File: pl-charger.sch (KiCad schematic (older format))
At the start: 16 parts

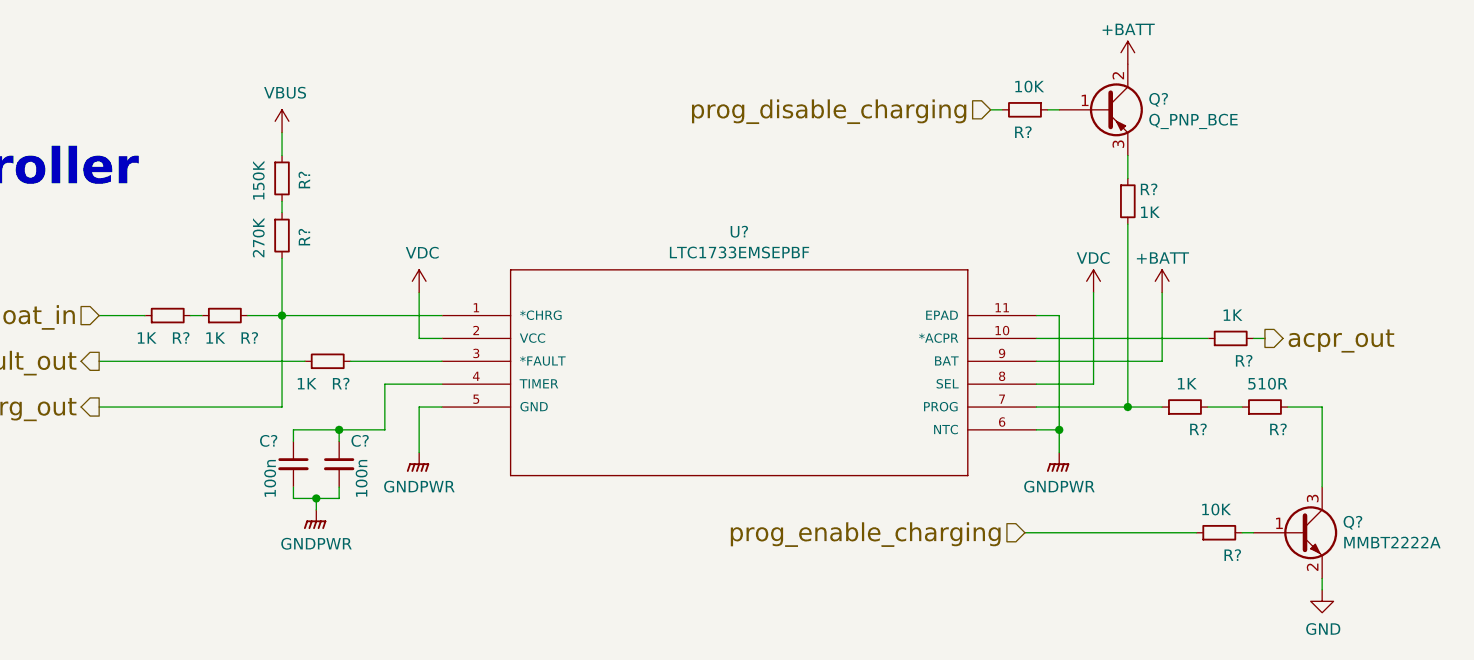
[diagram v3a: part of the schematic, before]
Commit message: Added component values
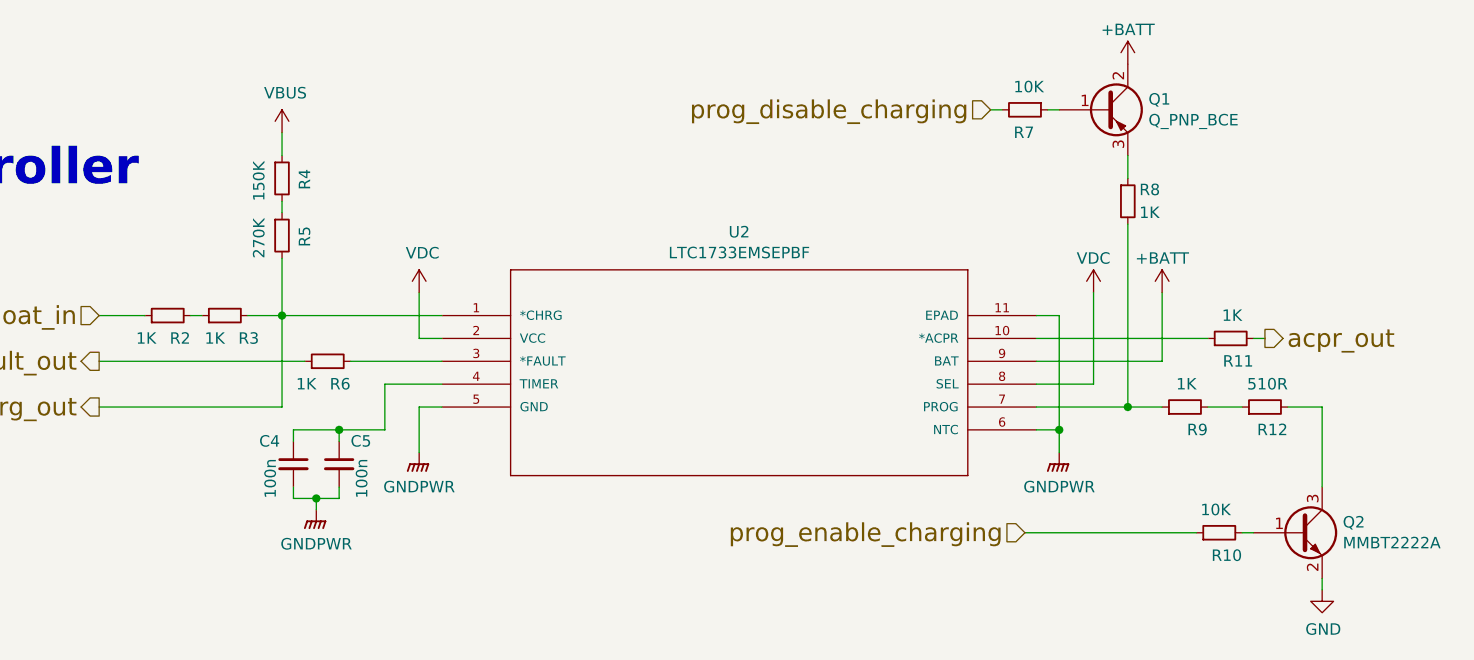
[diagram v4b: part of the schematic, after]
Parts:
- gave numbers to parts that had none: 16
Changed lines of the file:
@@
 $EndDescr
 $Comp
-L portable-light-rescue:R_Small-Device R?
+L portable-light-rescue:R_Small-Device R2
 U 1 1 5F378F6B
 P 3150 3500
-F 0 "R?" V 3050 3400 50  0000 L CNN
+F 0 "R2" V 3050 3400 50  0000 L CNN
 F 1 "1K" V 3050 3550 50  0000 L CNN
 F 2 "Resistor_SMD:R_0603_1608Metric_Pad1.05x0.95mm_HandSolder" H 3150 3500 50  0001 C CNN
@@
 $EndComp
 $Comp
-L portable-light-rescue:R_Small-Device R?
+L portable-light-rescue:R_Small-Device R3
 U 1 1 5F54FED1
 P 3400 3500
-F 0 "R?" V 3300 3350 50  0000 L CNN
+F 0 "R3" V 3300 3350 50  0000 L CNN
 F 1 "1K" V 3300 3500 50  0000 L CNN
 F 2 "Resistor_SMD:R_0603_1608Metric_Pad1.05x0.95mm_HandSolder" H 3400 3500 50  0001 C CNN
@@
 $EndComp
 $Comp
-L portable-light-rescue:VBUS-power #PWR?
+L portable-light-rescue:VBUS-power #PWR020
 U 1 1 5F15EA3E
 P 3650 2700
-F 0 "#PWR?" H 3650 2550 50  0001 C CNN
+F 0 "#PWR020" H 3650 2550 50  0001 C CNN
 F 1 "VBUS" H 3665 2873 50  0000 C CNN
 F 2 "" H 3650 2700 50  0001 C CNN
@@
 	2850 3500 3050 3500
 $Comp
-L portable-light-rescue:VDC-power #PWR?
+L portable-light-rescue:VDC-power #PWR022
 U 1 1 5F378F81
 P 4250 3400
-F 0 "#PWR?" H 4250 3300 50  0001 C CNN
+F 0 "#PWR022" H 4250 3300 50  0001 C CNN
 F 1 "VDC" H 4265 3573 50  0000 C CNN
 F 2 "" H 4250 3400 50  0001 C CNN
@@
 	4250 3600 4350 3600
 $Comp
-L portable-light-rescue:R_Small-Device R?
+L portable-light-rescue:R_Small-Device R11
 U 1 1 5F378F82
 P 7800 3600
-F 0 "R?" V 7700 3500 50  0000 L CNN
+F 0 "R11" V 7700 3500 50  0000 L CNN
 F 1 "1K" V 7900 3550 50  0000 L CNN
 F 2 "Resistor_SMD:R_0603_1608Metric_Pad1.05x0.95mm_HandSolder" H 7800 3600 50  0001 C CNN
@@
 	7900 3600 7950 3600
 $Comp
-L portable-light-rescue:+BATT-power #PWR?
+L portable-light-rescue:+BATT-power #PWR027
 U 1 1 5F378F86
 P 7500 3400
-F 0 "#PWR?" H 7500 3250 50  0001 C CNN
+F 0 "#PWR027" H 7500 3250 50  0001 C CNN
 F 1 "+BATT" H 7500 3550 50  0000 C CNN
 F 2 "" H 7500 3400 50  0001 C CNN
@@
 	7050 4000 6950 4000
 $Comp
-L portable-light-rescue:GNDPWR-power #PWR?
+L portable-light-rescue:GNDPWR-power #PWR024
 U 1 1 5F378F92
 P 7050 4100
-F 0 "#PWR?" H 7050 3900 50  0001 C CNN
+F 0 "#PWR024" H 7050 3900 50  0001 C CNN
 F 1 "GNDPWR" H 7050 3950 50  0000 C CNN
 F 2 "" H 7050 4050 50  0001 C CNN
@@
 Connection ~ 7050 4000
 $Comp
-L portable-light-rescue:GNDPWR-power #PWR?
+L portable-light-rescue:GNDPWR-power #PWR023
 U 1 1 5F54FEEB
 P 4250 4100
-F 0 "#PWR?" H 4250 3900 50  0001 C CNN
+F 0 "#PWR023" H 4250 3900 50  0001 C CNN
 F 1 "GNDPWR" H 4250 3950 50  0000 C CNN
 F 2 "" H 4250 4050 50  0001 C CNN
@@
 	4250 3900 4250 4100
 $Comp
-L portable-light-rescue:R_Small-Device R?
+L portable-light-rescue:R_Small-Device R6
 U 1 1 5F1F45F5
 P 3850 3700
-F 0 "R?" V 3750 3600 50  0000 L CNN
+F 0 "R6" V 3750 3600 50  0000 L CNN
 F 1 "1K" V 3750 3750 50  0000 L CNN
 F 2 "Resistor_SMD:R_0603_1608Metric_Pad1.05x0.95mm_HandSolder" H 3850 3700 50  0001 C CNN
@@
 	7050 3500 7050 4000
 $Comp
-L portable-light-rescue:R_Small-Device R?
+L portable-light-rescue:R_Small-Device R9
 U 1 1 5F2794F2
 P 7600 3900
-F 0 "R?" V 7500 3800 50  0000 L CNN
+F 0 "R9" V 7500 3800 50  0000 L CNN
 F 1 "1K" V 7700 3850 50  0000 L CNN
 F 2 "Resistor_SMD:R_0603_1608Metric_Pad1.05x0.95mm_HandSolder" H 7600 3900 50  0001 C CNN
@@
 $EndComp
 $Comp
-L portable-light-rescue:R_Small-Device R?
+L portable-light-rescue:R_Small-Device R12
 U 1 1 5F378F9A
 P 7950 3900
-F 0 "R?" V 7850 3800 50  0000 L CNN
+F 0 "R12" V 7850 3800 50  0000 L CNN
 F 1 "510R" V 8050 3800 50  0000 L CNN
 F 2 "Resistor_SMD:R_0805_2012Metric_Pad1.15x1.40mm_HandSolder" H 7950 3900 50  0001 C CNN
@@
 $EndComp
 $Comp
-L portable-light-rescue:C_Small-Device C?
+L portable-light-rescue:C_Small-Device C5
 U 1 1 5F378F9E
 P 3900 4150
-F 0 "C?" H 3950 4250 50  0000 L CNN
+F 0 "C5" H 3950 4250 50  0000 L CNN
 F 1 "100n" V 3600 4000 50  0000 L CNN
 F 2 "Capacitor_SMD:C_1206_3216Metric_Pad1.42x1.75mm_HandSolder" H 3900 4150 50  0001 C CNN
@@
 $EndComp
 $Comp
-L portable-light-rescue:C_Small-Device C?
+L portable-light-rescue:C_Small-Device C4
 U 1 1 5F290824
 P 3700 4150
-F 0 "C?" H 3550 4250 50  0000 L CNN
+F 0 "C4" H 3550 4250 50  0000 L CNN
 F 1 "100n" V 4000 4000 50  0000 L CNN
 F 2 "Capacitor_SMD:C_1206_3216Metric_Pad1.42x1.75mm_HandSolder" H 3700 4150 50  0001 C CNN
@@
 	3800 4300 3900 4300
 $Comp
-L portable-light-rescue:R_Small-Device R?
+L portable-light-rescue:R_Small-Device R10
 U 1 1 5F317001
 P 7750 4450
-F 0 "R?" V 7650 4350 50  0000 L CNN
+F 0 "R10" V 7650 4350 50  0000 L CNN
 F 1 "10K" V 7850 4400 50  0000 L CNN
 F 2 "Resistor_SMD:R_1206_3216Metric_Pad1.42x1.75mm_HandSolder" H 7750 4450 50  0001 C CNN
@@
 	8050 3900 8200 3900
 $Comp
-L portable-light-rescue:R_Small-Device R?
+L portable-light-rescue:R_Small-Device R8
 U 1 1 5F378FB3
 P 7350 3000
-F 0 "R?" H 7400 3050 50  0000 L CNN
+F 0 "R8" H 7400 3050 50  0000 L CNN
 F 1 "1K" H 7400 2950 50  0000 L CNN
 F 2 "Resistor_SMD:R_0603_1608Metric_Pad1.05x0.95mm_HandSolder" H 7350 3000 50  0001 C CNN
@@
 Charge controller
 $Comp
-L portable-light-rescue:MMBT3904-Transistor_BJT Q?
+L portable-light-rescue:MMBT3904-Transistor_BJT Q2
 U 1 1 5F378FE9
 P 8100 4450
-F 0 "Q?" H 8290 4496 50  0000 L CNN
+F 0 "Q2" H 8290 4496 50  0000 L CNN
 F 1 "MMBT2222A" H 8290 4405 50  0000 L CNN
 F 2 "Package_TO_SOT_SMD:SOT-23" H 8300 4375 50  0001 L CIN
@@
 $EndComp
 $Comp
-L portable-light-rescue:LTC1733EMSEPBF-LTC1733 U?
+L portable-light-rescue:LTC1733EMSEPBF-LTC1733 U2
 U 1 1 5F378FEA
 P 4350 3500
-F 0 "U?" H 5650 3865 50  0000 C CNN
+F 0 "U2" H 5650 3865 50  0000 C CNN
 F 1 "LTC1733EMSEPBF" H 5650 3774 50  0000 C CNN
 F 2 "UniX_Generic:MSOP-10_MSE" H 4350 3500 50  0001 L BNN
@@
 $EndComp
 $Comp
-L portable-light-rescue:GNDPWR-power #PWR?
+L portable-light-rescue:GNDPWR-power #PWR021
 U 1 1 5F54FEE8
 P 3800 4350
-F 0 "#PWR?" H 3800 4150 50  0001 C CNN
+F 0 "#PWR021" H 3800 4150 50  0001 C CNN
 F 1 "GNDPWR" H 3800 4200 50  0000 C CNN
 F 2 "" H 3800 4300 50  0001 C CNN
@@
 $EndComp
 $Comp
-L portable-light-rescue:GND-power #PWR?
+L portable-light-rescue:GND-power #PWR028
 U 1 1 5F351CC6
 P 8200 4700
-F 0 "#PWR?" H 8200 4450 50  0001 C CNN
+F 0 "#PWR028" H 8200 4450 50  0001 C CNN
 F 1 "GND" H 8205 4527 50  0000 C CNN
 F 2 "" H 8200 4700 50  0001 C CNN
@@
 	3650 2700 3650 2800
 $Comp
-L portable-light-rescue:VDC-power #PWR?
+L portable-light-rescue:VDC-power #PWR025
 U 1 1 5F378F8D
 P 7200 3400
-F 0 "#PWR?" H 7200 3300 50  0001 C CNN
+F 0 "#PWR025" H 7200 3300 50  0001 C CNN
 F 1 "VDC" H 7200 3550 50  0000 C CNN
 F 2 "" H 7200 3400 50  0001 C CNN
@@
 	7500 3700 7500 3400
 $Comp
-L portable-light-rescue:R_Small-Device R?
+L portable-light-rescue:R_Small-Device R4
 U 1 1 5F65CDB9
 P 3650 2900
-F 0 "R?" V 3750 2850 50  0000 L CNN
+F 0 "R4" V 3750 2850 50  0000 L CNN
 F 1 "150K" V 3550 2800 50  0000 L CNN
 F 2 "Resistor_SMD:R_0603_1608Metric_Pad1.05x0.95mm_HandSolder" H 3650 2900 50  0001 C CNN
@@
 $EndComp
 $Comp
-L portable-light-rescue:R_Small-Device R?
+L portable-light-rescue:R_Small-Device R5
 U 1 1 5F65EB20
 P 3650 3150
-F 0 "R?" V 3750 3100 50  0000 L CNN
+F 0 "R5" V 3750 3100 50  0000 L CNN
 F 1 "270K" V 3550 3050 50  0000 L CNN
 F 2 "Resistor_SMD:R_0603_1608Metric_Pad1.05x0.95mm_HandSolder" H 3650 3150 50  0001 C CNN
@@
 fault_out
 $Comp
-L Device:Q_PNP_BCE Q?
+L Device:Q_PNP_BCE Q1
 U 1 1 5F5A7610
 P 7250 2600
-F 0 "Q?" H 7440 2646 50  0000 L CNN
+F 0 "Q1" H 7440 2646 50  0000 L CNN
 F 1 "Q_PNP_BCE" H 7440 2555 50  0000 L CNN
 F 2 "" H 7450 2700 50  0001 C CNN
@@
 $EndComp
 $Comp
-L portable-light-rescue:+BATT-power #PWR?
+L portable-light-rescue:+BATT-power #PWR026
 U 1 1 5F5AB657
 P 7350 2400
-F 0 "#PWR?" H 7350 2250 50  0001 C CNN
+F 0 "#PWR026" H 7350 2250 50  0001 C CNN
 F 1 "+BATT" H 7350 2550 50  0000 C CNN
 F 2 "" H 7350 2400 50  0001 C CNN
@@
 $EndComp
 $Comp
-L portable-light-rescue:R_Small-Device R?
+L portable-light-rescue:R_Small-Device R7
 U 1 1 5F5AE6E8
 P 6900 2600
-F 0 "R?" V 7000 2550 50  0000 L CNN
+F 0 "R7" V 7000 2550 50  0000 L CNN
 F 1 "10K" V 6800 2550 50  0000 L CNN
 F 2 "Resistor_SMD:R_0603_1608Metric_Pad1.05x0.95mm_HandSolder" H 6900 2600 50  0001 C CNN

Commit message: Schematics redesigned and fixed
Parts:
- added C4: 10u, Capacitor_THT:C_Radial_D5.0mm_H7.0mm_P2.00mm, symbol portable-light-rescue:C_Small-Device
- added J10: Charger, Connector_PinHeader_2.54mm:PinHeader_1x02_P2.54mm_Vertical, symbol portable-light-rescue:Conn_01x02-Connector_Generic
- Q1: footprint (none) -> Package_TO_SOT_SMD:SOT-23
- renumbered C4 to C2, C5 to C3, U2 to U1
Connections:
- net labels added: +5V, +BATT-2, +CHARGER, GND-CHARGER
- net labels removed: +BATT, GND, GNDPWR, VBUS, VDC
- wire segments 48 -> 56
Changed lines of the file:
@@
 	0    -1   -1   0
-$EndComp
-$Comp
-L portable-light-rescue:VBUS-power #PWR020
-U 1 1 5F15EA3E
-P 3650 2700
-F 0 "#PWR020" H 3650 2550 50  0001 C CNN
-F 1 "VBUS" H 3665 2873 50  0000 C CNN
-F 2 "" H 3650 2700 50  0001 C CNN
-F 3 "" H 3650 2700 50  0001 C CNN
-	1    3650 2700
-	1    0    0    -1
 $EndComp
 Wire Wire Line
@@
 Wire Wire Line
 	2850 3500 3050 3500
-$Comp
-L portable-light-rescue:VDC-power #PWR022
-U 1 1 5F378F81
-P 4250 3400
-F 0 "#PWR022" H 4250 3300 50  0001 C CNN
-F 1 "VDC" H 4265 3573 50  0000 C CNN
-F 2 "" H 4250 3400 50  0001 C CNN
-F 3 "" H 4250 3400 50  0001 C CNN
-	1    4250 3400
-	1    0    0    -1
-$EndComp
 Wire Wire Line
 	4250 3400 4250 3600
@@
 Wire Wire Line
 	7900 3600 7950 3600
-$Comp
-L portable-light-rescue:+BATT-power #PWR027
-U 1 1 5F378F86
-P 7500 3400
-F 0 "#PWR027" H 7500 3250 50  0001 C CNN
-F 1 "+BATT" H 7500 3550 50  0000 C CNN
-F 2 "" H 7500 3400 50  0001 C CNN
-F 3 "" H 7500 3400 50  0001 C CNN
-	1    7500 3400
-	1    0    0    -1
-$EndComp
 Wire Wire Line
 	6950 3800 7200 3800
@@
 Wire Wire Line
 	7050 4000 6950 4000
-$Comp
-L portable-light-rescue:GNDPWR-power #PWR024
-U 1 1 5F378F92
-P 7050 4100
-F 0 "#PWR024" H 7050 3900 50  0001 C CNN
-F 1 "GNDPWR" H 7050 3950 50  0000 C CNN
-F 2 "" H 7050 4050 50  0001 C CNN
-F 3 "" H 7050 4050 50  0001 C CNN
-	1    7050 4100
-	1    0    0    -1
-$EndComp
 Wire Wire Line
 	7050 4000 7050 4100
 Connection ~ 7050 4000
-$Comp
-L portable-light-rescue:GNDPWR-power #PWR023
-U 1 1 5F54FEEB
-P 4250 4100
-F 0 "#PWR023" H 4250 3900 50  0001 C CNN
-F 1 "GNDPWR" H 4250 3950 50  0000 C CNN
-F 2 "" H 4250 4050 50  0001 C CNN
-F 3 "" H 4250 4050 50  0001 C CNN
-	1    4250 4100
-	1    0    0    -1
-$EndComp
 Wire Wire Line
 	4350 3900 4250 3900
@@
 $EndComp
 $Comp
-L portable-light-rescue:C_Small-Device C5
+L portable-light-rescue:C_Small-Device C3
 U 1 1 5F378F9E
 P 3900 4150
-F 0 "C5" H 3950 4250 50  0000 L CNN
+F 0 "C3" H 3950 4250 50  0000 L CNN
 F 1 "100n" V 3600 4000 50  0000 L CNN
 F 2 "Capacitor_SMD:C_1206_3216Metric_Pad1.42x1.75mm_HandSolder" H 3900 4150 50  0001 C CNN
@@
 $EndComp
 $Comp
-L portable-light-rescue:C_Small-Device C4
+L portable-light-rescue:C_Small-Device C2
 U 1 1 5F290824
 P 3700 4150
-F 0 "C4" H 3550 4250 50  0000 L CNN
+F 0 "C2" H 3550 4250 50  0000 L CNN
 F 1 "100n" V 4000 4000 50  0000 L CNN
 F 2 "Capacitor_SMD:C_1206_3216Metric_Pad1.42x1.75mm_HandSolder" H 3700 4150 50  0001 C CNN
@@
 	7350 3900 7500 3900
 Wire Wire Line
-	7650 4450 6900 4450
-Wire Wire Line
 	8200 3900 8200 4250
 Wire Wire Line
@@
 $EndComp
 $Comp
-L portable-light-rescue:LTC1733EMSEPBF-LTC1733 U2
+L portable-light-rescue:LTC1733EMSEPBF-LTC1733 U1
 U 1 1 5F378FEA
 P 4350 3500
-F 0 "U2" H 5650 3865 50  0000 C CNN
+F 0 "U1" H 5650 3865 50  0000 C CNN
 F 1 "LTC1733EMSEPBF" H 5650 3774 50  0000 C CNN
 F 2 "UniX_Generic:MSOP-10_MSE" H 4350 3500 50  0001 L BNN
@@
 	1    0    0    -1
 $EndComp
-$Comp
-L portable-light-rescue:GNDPWR-power #PWR021
-U 1 1 5F54FEE8
-P 3800 4350
-F 0 "#PWR021" H 3800 4150 50  0001 C CNN
-F 1 "GNDPWR" H 3800 4200 50  0000 C CNN
-F 2 "" H 3800 4300 50  0001 C CNN
-F 3 "" H 3800 4300 50  0001 C CNN
-	1    3800 4350
-	1    0    0    -1
-$EndComp
-$Comp
-L portable-light-rescue:GND-power #PWR028
-U 1 1 5F351CC6
-P 8200 4700
-F 0 "#PWR028" H 8200 4450 50  0001 C CNN
-F 1 "GND" H 8205 4527 50  0000 C CNN
-F 2 "" H 8200 4700 50  0001 C CNN
-F 3 "" H 8200 4700 50  0001 C CNN
-	1    8200 4700
-	1    0    0    -1
-$EndComp
 Wire Wire Line
 	3650 3250 3650 3500
 Wire Wire Line
 	3650 2700 3650 2800
-$Comp
-L portable-light-rescue:VDC-power #PWR025
-U 1 1 5F378F8D
-P 7200 3400
-F 0 "#PWR025" H 7200 3300 50  0001 C CNN
-F 1 "VDC" H 7200 3550 50  0000 C CNN
-F 2 "" H 7200 3400 50  0001 C CNN
-F 3 "" H 7200 3400 50  0001 C CNN
-	1    7200 3400
-	1    0    0    -1
-$EndComp
 Wire Wire Line
 	7200 3800 7200 3400
-Wire Wire Line
-	7500 3700 7500 3400
 $Comp
 L portable-light-rescue:R_Small-Device R4
@@
 Wire Wire Line
 	3650 3050 3650 3000
-Text HLabel 6900 4450 0    79   Input ~ 0
+Text HLabel 7550 4450 3    79   Input ~ 0
 prog_enable_charging
 Text HLabel 6750 2600 0    79   Input ~ 0
@@
 F 0 "Q1" H 7440 2646 50  0000 L CNN
 F 1 "Q_PNP_BCE" H 7440 2555 50  0000 L CNN
-F 2 "" H 7450 2700 50  0001 C CNN
+F 2 "Package_TO_SOT_SMD:SOT-23" H 7450 2700 50  0001 C CNN
 F 3 "~" H 7250 2600 50  0001 C CNN
 	1    7250 2600
-	1    0    0    -1
-$EndComp
-$Comp
-L portable-light-rescue:+BATT-power #PWR026
-U 1 1 5F5AB657
-P 7350 2400
-F 0 "#PWR026" H 7350 2250 50  0001 C CNN
-F 1 "+BATT" H 7350 2550 50  0000 C CNN
-F 2 "" H 7350 2400 50  0001 C CNN
-F 3 "" H 7350 2400 50  0001 C CNN
-	1    7350 2400
 	1    0    0    -1
 $EndComp
@@
 Wire Wire Line
 	7350 3900 7350 3100
+Text GLabel 7200 3400 1    39   UnSpc ~ 0
++CHARGER
+Text GLabel 7350 2400 1    39   UnSpc ~ 0
++BATT-2
+Text GLabel 3650 2700 1    39   UnSpc ~ 0
++5V
+Text GLabel 4250 3400 1    39   UnSpc ~ 0
++CHARGER
+Text GLabel 3800 4350 3    39   UnSpc ~ 0
+GND-CHARGER
+Text GLabel 8200 4700 3    39   UnSpc ~ 0
+GND-CHARGER
+Text GLabel 4250 4100 3    39   UnSpc ~ 0
+GND-CHARGER
+Text GLabel 7050 4100 3    39   UnSpc ~ 0
+GND-CHARGER
+Wire Wire Line
+	7550 4450 7650 4450
+$Comp
+L portable-light-rescue:Conn_01x02-Connector_Generic J?
+U 1 1 5F88BAE0
+P 5700 5100
+AR Path="/5F88BAE0" Ref="J?"  Part="1"
+AR Path="/5F378869/5F88BAE0" Ref="J?"  Part="1"
+AR Path="/5F377120/5F88BAE0" Ref="J10"  Part="1"
+F 0 "J10" V 5600 5050 50  0000 L CNN
+F 1 "Charger" V 5800 4850 50  0000 L CNN
+F 2 "Connector_PinHeader_2.54mm:PinHeader_1x02_P2.54mm_Vertical" H 5700 5100 50  0001 C CNN
+F 3 "~" H 5700 5100 50  0001 C CNN
+	1    5700 5100
+	0    1    1    0
+$EndComp
+Wire Wire Line
+	5600 4850 5600 4900
+Text GLabel 5300 4850 0    39   UnSpc ~ 0
+GND-CHARGER
+$Comp
+L power:PWR_FLAG #FLG06
+U 1 1 5F8C1055
+P 5400 4850
+F 0 "#FLG06" H 5400 4925 50  0001 C CNN
+F 1 "PWR_FLAG" H 5400 5023 50  0000 C CNN
+F 2 "" H 5400 4850 50  0001 C CNN
+F 3 "~" H 5400 4850 50  0001 C CNN
+	1    5400 4850
+	1    0    0    -1
+$EndComp
+Text GLabel 6000 4850 2    39   UnSpc ~ 0
++CHARGER
+Wire Wire Line
+	5700 4900 5700 4850
+Wire Wire Line
+	5300 4850 5400 4850
+Wire Wire Line
+	5700 4850 5850 4850
+$Comp
+L power:PWR_FLAG #FLG07
+U 1 1 5F8CCEC0
+P 5850 4850
+F 0 "#FLG07" H 5850 4925 50  0001 C CNN
+F 1 "PWR_FLAG" H 5850 5023 50  0000 C CNN
+F 2 "" H 5850 4850 50  0001 C CNN
+F 3 "~" H 5850 4850 50  0001 C CNN
+	1    5850 4850
+	1    0    0    -1
+$EndComp
+Connection ~ 5850 4850
+Wire Wire Line
+	5850 4850 6000 4850
+Connection ~ 5400 4850
+Wire Wire Line
+	5400 4850 5600 4850
+$Comp
+L portable-light-rescue:C_Small-Device C?
+U 1 1 5F8D5922
+P 5650 5550
+AR Path="/5F8D5922" Ref="C?"  Part="1"
+AR Path="/5F378869/5F8D5922" Ref="C?"  Part="1"
+AR Path="/5F377120/5F8D5922" Ref="C4"  Part="1"
+F 0 "C4" H 5700 5650 50  0000 L CNN
+F 1 "10u" V 5500 5500 50  0000 L CNN
+F 2 "Capacitor_THT:C_Radial_D5.0mm_H7.0mm_P2.00mm" H 5650 5550 50  0001 C CNN
+F 3 "~" H 5650 5550 50  0001 C CNN
+	1    5650 5550
+	0    1    1    0
+$EndComp
+Text GLabel 6000 5550 2    39   UnSpc ~ 0
++CHARGER
+Text GLabel 5300 5550 0    39   UnSpc ~ 0
+GND-CHARGER
+Wire Wire Line
+	5750 5550 6000 5550
+Wire Wire Line
+	5300 5550 5550 5550
+Text GLabel 7500 3500 1    39   UnSpc ~ 0
++BATT-2
+Wire Wire Line
+	7500 3500 7500 3700
 $EndSCHEMATC
